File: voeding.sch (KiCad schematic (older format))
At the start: 38 parts

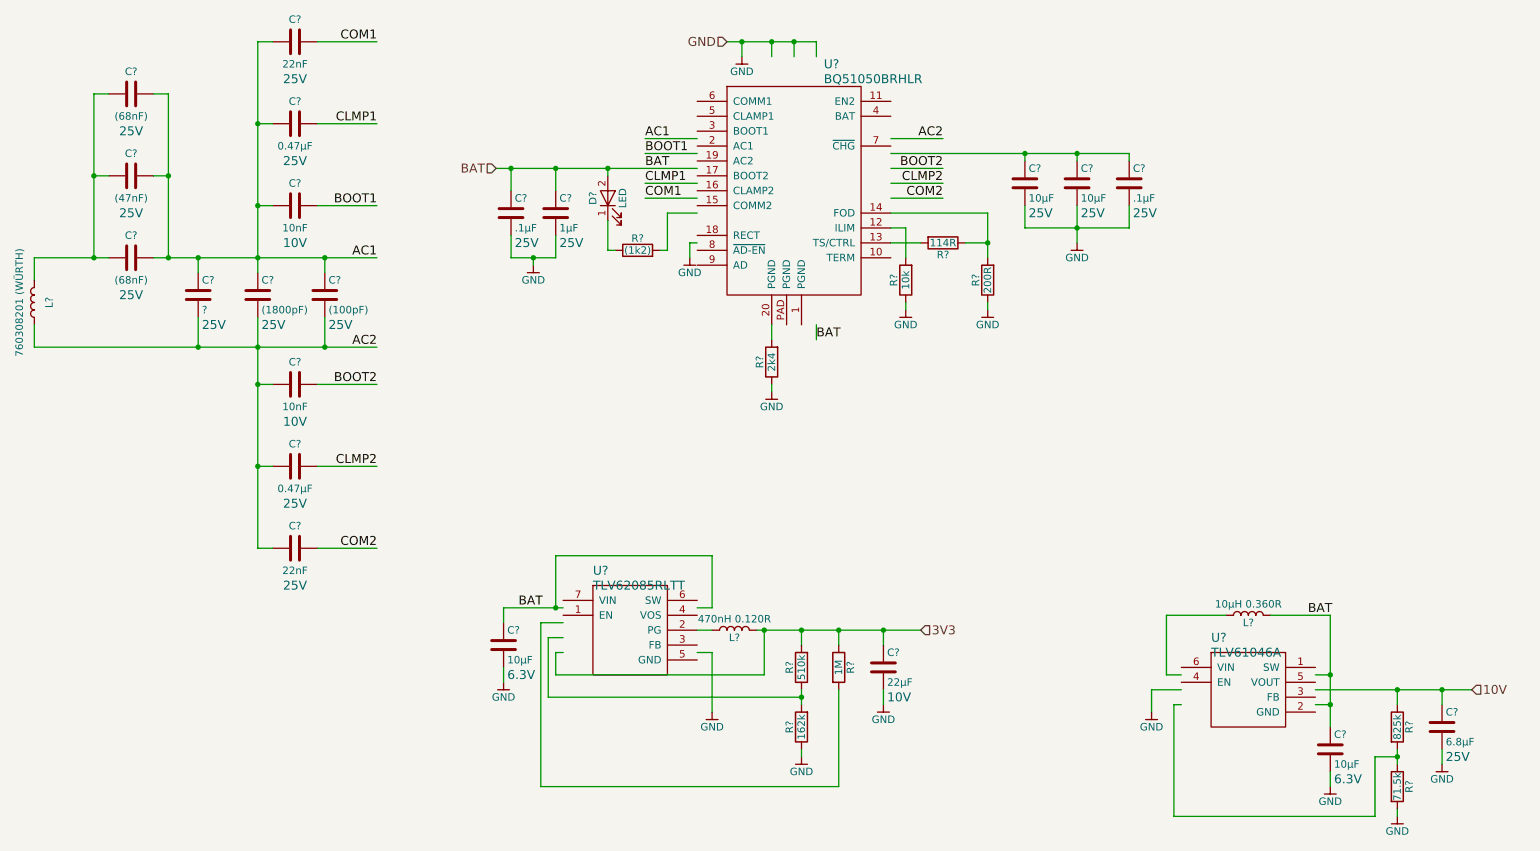
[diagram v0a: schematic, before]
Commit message: redid schematic symbols
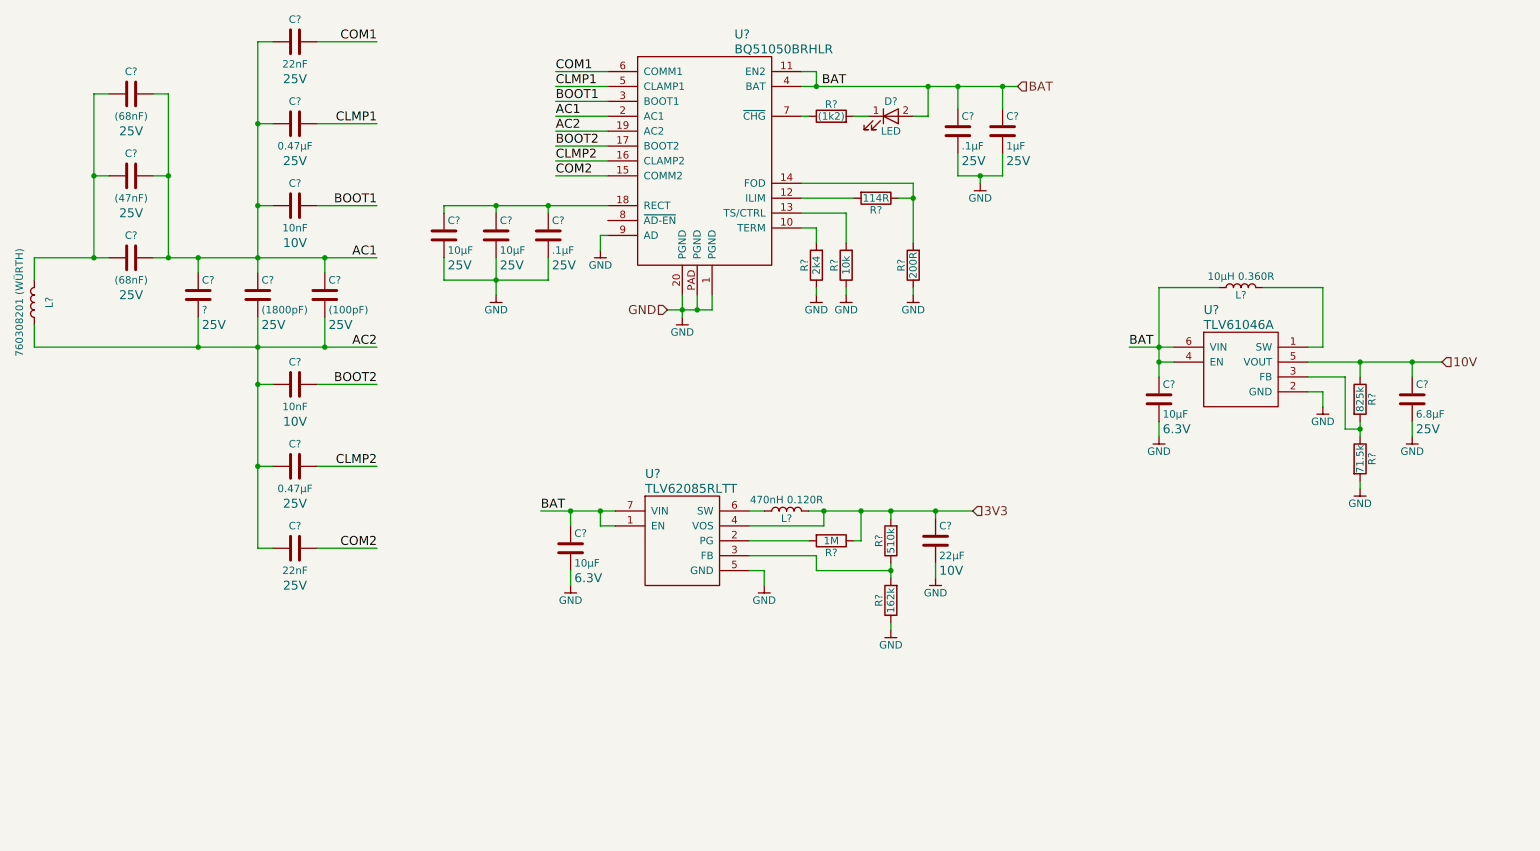
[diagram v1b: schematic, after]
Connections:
- wire segments 125 -> 158
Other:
- moved on the sheet: C?, D?, L?, R?, U?

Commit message: added HC-05 symbol
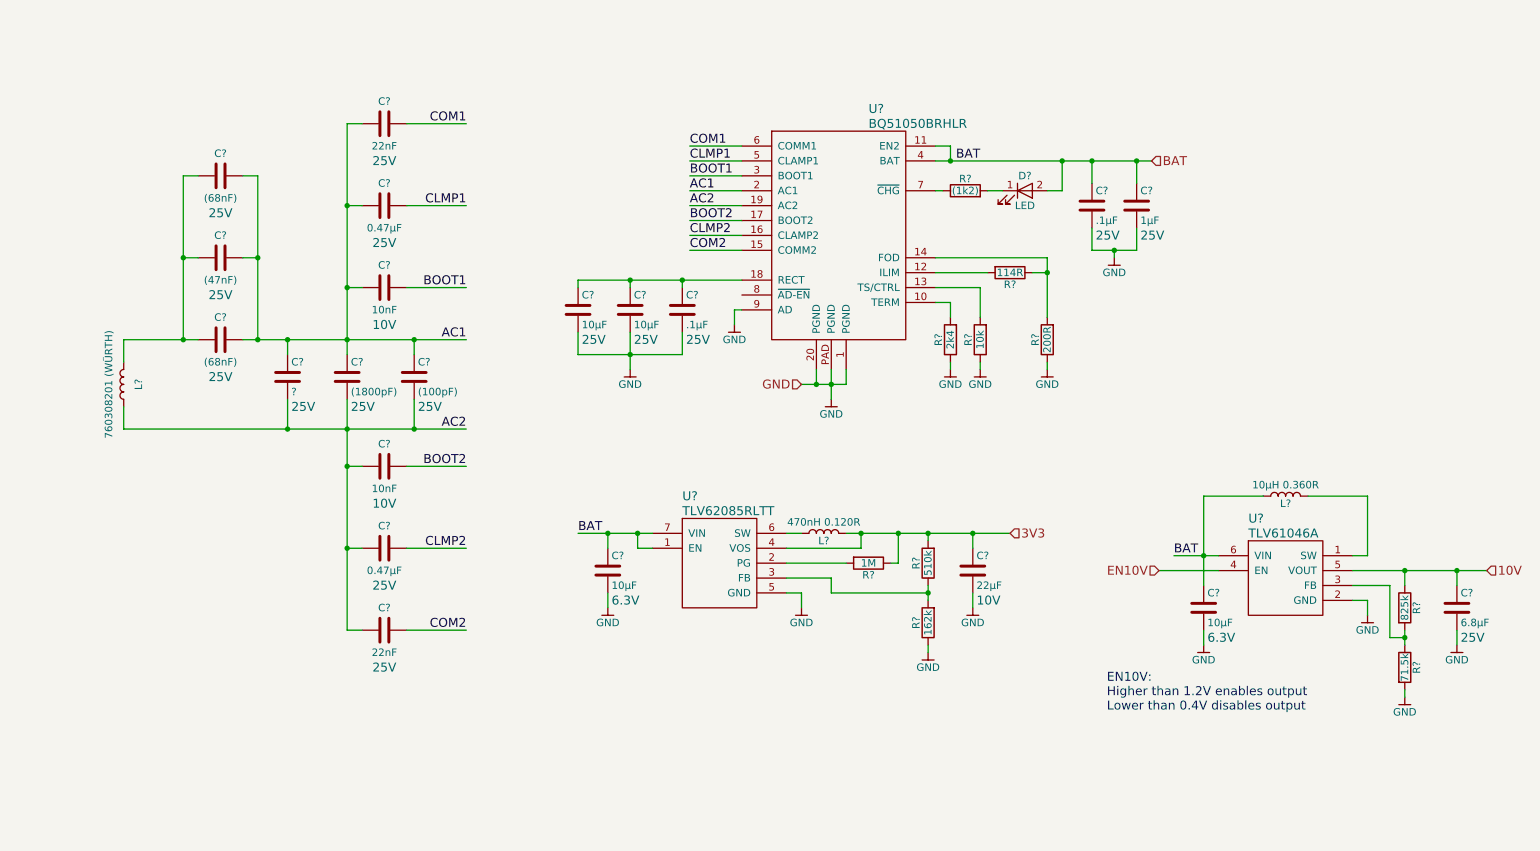
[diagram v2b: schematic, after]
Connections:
- net BAT: no longer U?.4 (EN)
- new net EN10V: U?.4 (EN)
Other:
- note added: "EN10V:\nHigher than 1.2V enables output\nLower than 0.4V disables output"
- moved on the sheet: C?, D?, L?, R?, U?
